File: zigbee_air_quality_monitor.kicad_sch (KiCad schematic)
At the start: 21 parts, among them J1 USB_C_Receptacle_USB2.0, J2 Conn_02x02_Odd_Even, SW1 PWR_BTN, U1 BT840, U2 PRTR5V0U2F, U3 XC6206P332MR, U4 SCD41-D-R2

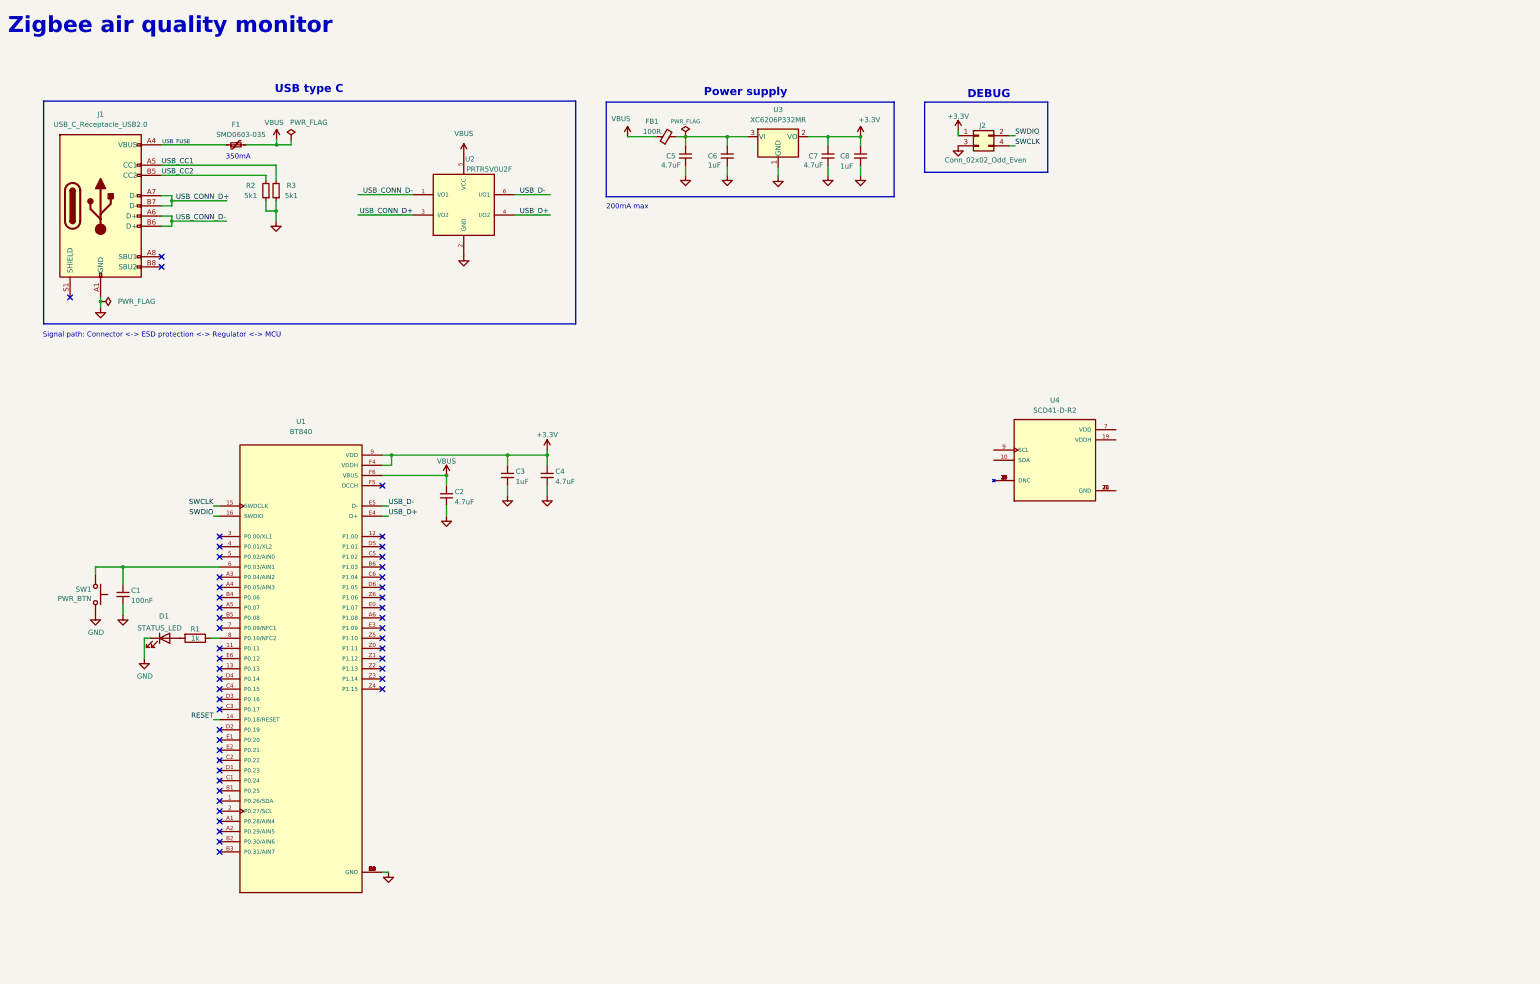
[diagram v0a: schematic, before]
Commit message: Finished schematics, added 3D models
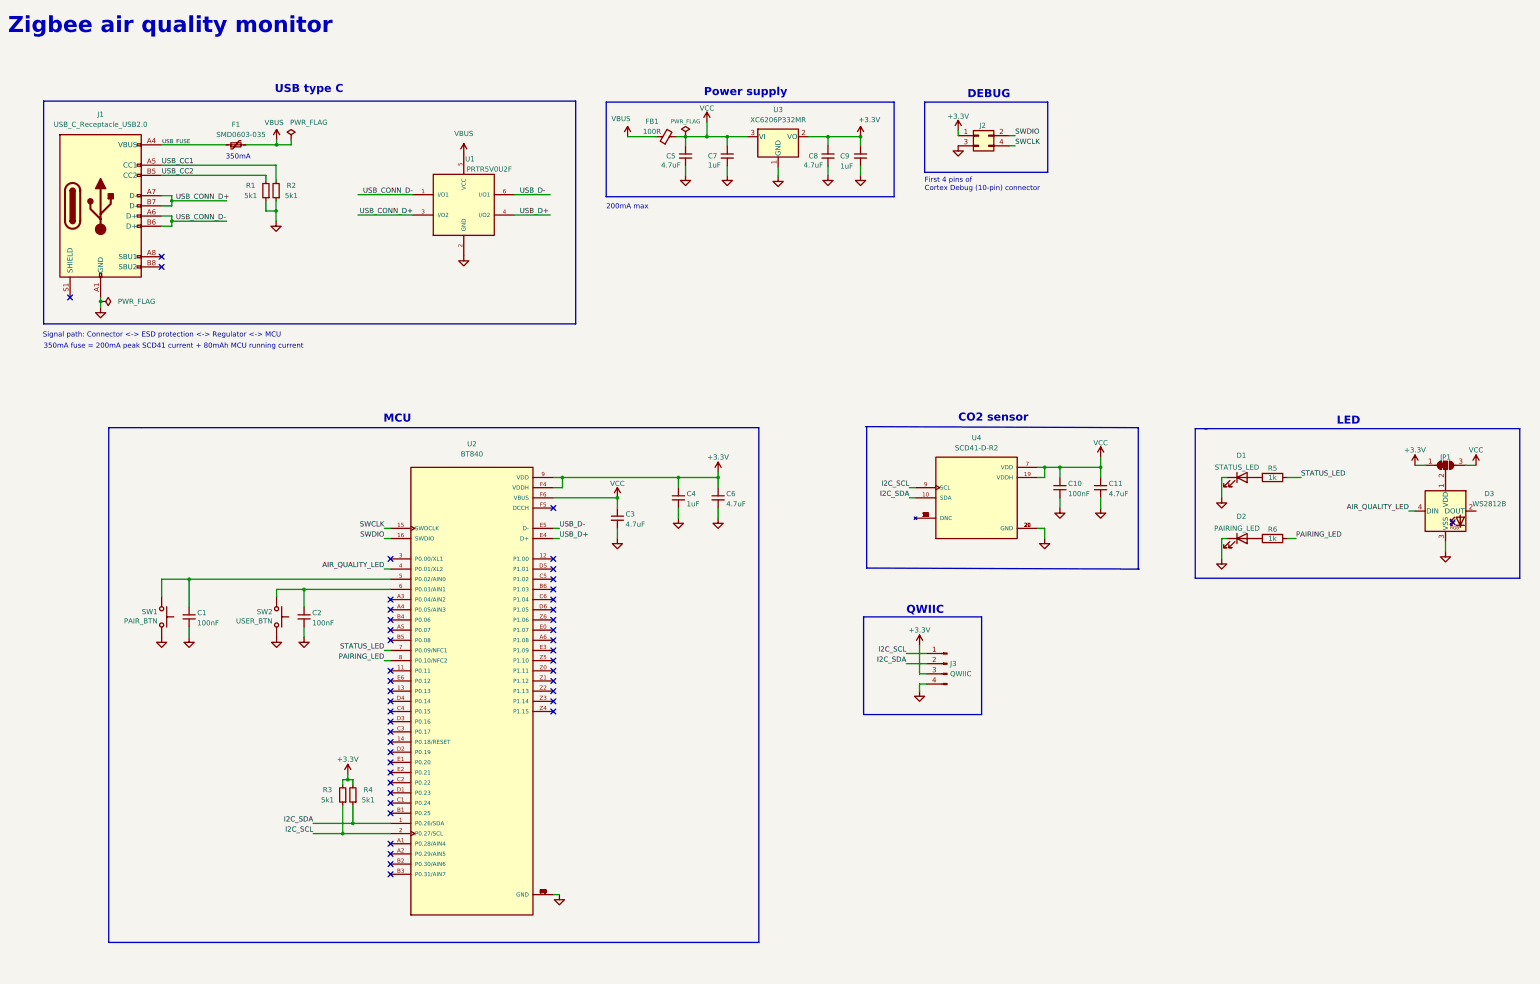
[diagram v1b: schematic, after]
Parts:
- added C1, C10: 100nF, Capacitor_SMD:C_0603_1608Metric, symbol Device:C_Small
- added C11: 4.7uF, Capacitor_SMD:C_0603_1608Metric, symbol Device:C_Small
- added D1: STATUS_LED, LED_SMD:LED_0603_1608Metric, symbol Device:LED
- added D3: WS2812B, LED_SMD:LED_WS2812B-2020_PLCC4_2.0x2.0mm, symbol LED:WS2812B
- added J3: QWIIC, Connector_JST:JST_SH_BM04B-SRSS-TB_1x04-1MP_P1.00mm_Vertical, symbol Connector:Conn_01x04_Male
- added JP1: SolderJumper_3_Bridged12, Jumper:SolderJumper-3_P1.3mm_Open_RoundedPad1.0x1.5mm, symbol Jumper:SolderJumper_3_Bridged12
- added R3, R4: 5k1, Resistor_SMD:R_0603_1608Metric, symbol Device:R_Small
- added R5: 1k, Resistor_SMD:R_0603_1608Metric, symbol Device:R
- added SW1: PAIR_BTN, Button_Switch_SMD:SW_Push_SPST_NO_Alps_SKRK, symbol Switch:SW_Push
- D2: renamed from D1; value STATUS_LED -> PAIRING_LED
- SW2: renamed from SW1; value PWR_BTN -> USER_BTN; footprint Button_Switch_SMD:SW_Push_1P1T_NO_6x6mm_H9.5mm -> Button_Switch_SMD:SW_Push_SPST_NO_Alps_SKRK; LCSC Part (none) -> C115357
- renumbered C1 to C2, C2 to C3, C3 to C4, C4 to C6, C6 to C7, C7 to C8, C8 to C9, R2 to R1, R3 to R2, R1 to R6, U2 to U1, U1 to U2
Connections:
- net +3.3V: now also J3.3 (Pin_3), JP1.1 (A), R3.2, R4.2
- net GND: now also U4.20 (GND), U4.21 (GND), U4.6 (GND), C1.2, C10.2, C11.2, D1.1 (K), D3.3 (VSS), J3.4 (Pin_4), SW1.2
- net VBUS: no longer C3.1, U2.F6 (VBUS)
- net VCC: now reaches C5.1, C7.1, FB1.2, U3.3 (VI)
- net VCC: now also C3.1, U2.F6 (VBUS), U4.19 (VDDH), U4.7 (VDD), C10.1, C11.1, JP1.3 (B)
- net I2C_SDA: now reaches U2.1 (P0.26/SDA)
- net I2C_SDA: now also U4.10 (SDA), J3.2 (Pin_2), R4.1
- net I2C_SCL: now reaches U2.2 (P0.27/SCL)
- net I2C_SCL: now also U4.9 (SCL), J3.1 (Pin_1), R3.1
- net AIR_QUALITY_LED: now reaches U2.4 (P0.01/XL2)
- net AIR_QUALITY_LED: now also D3.4 (DIN)
- net at U2.5 (P0.02/AIN0): now also C1.1, SW1.1
- net STATUS_LED: now reaches U2.7 (P0.09/NFC1)
- net STATUS_LED: now also R5.1
- net PAIRING_LED: now reaches R6.1, U2.8 (P0.10/NFC2)
- net RESET: no longer names the net of U2.14 (P0.18/RESET)
- new net: D3.1 (VDD), JP1.2 (C)
- new net: D1.2 (A), R5.2
- no-connect marks 49 -> 46
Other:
- note added: "350mA fuse = 200mA peak SCD41 current + 80mAh MCU running current"
- note added: "CO2 sensor"
- note added: "First 4 pins of Cortex Debug (10-pin) connector"
- note added: "LED"
- note added: "MCU"
- note added: "QWIIC"
- moved on the sheet: C2, C3, C4, C6, D2, R6, SW2, U2, U4

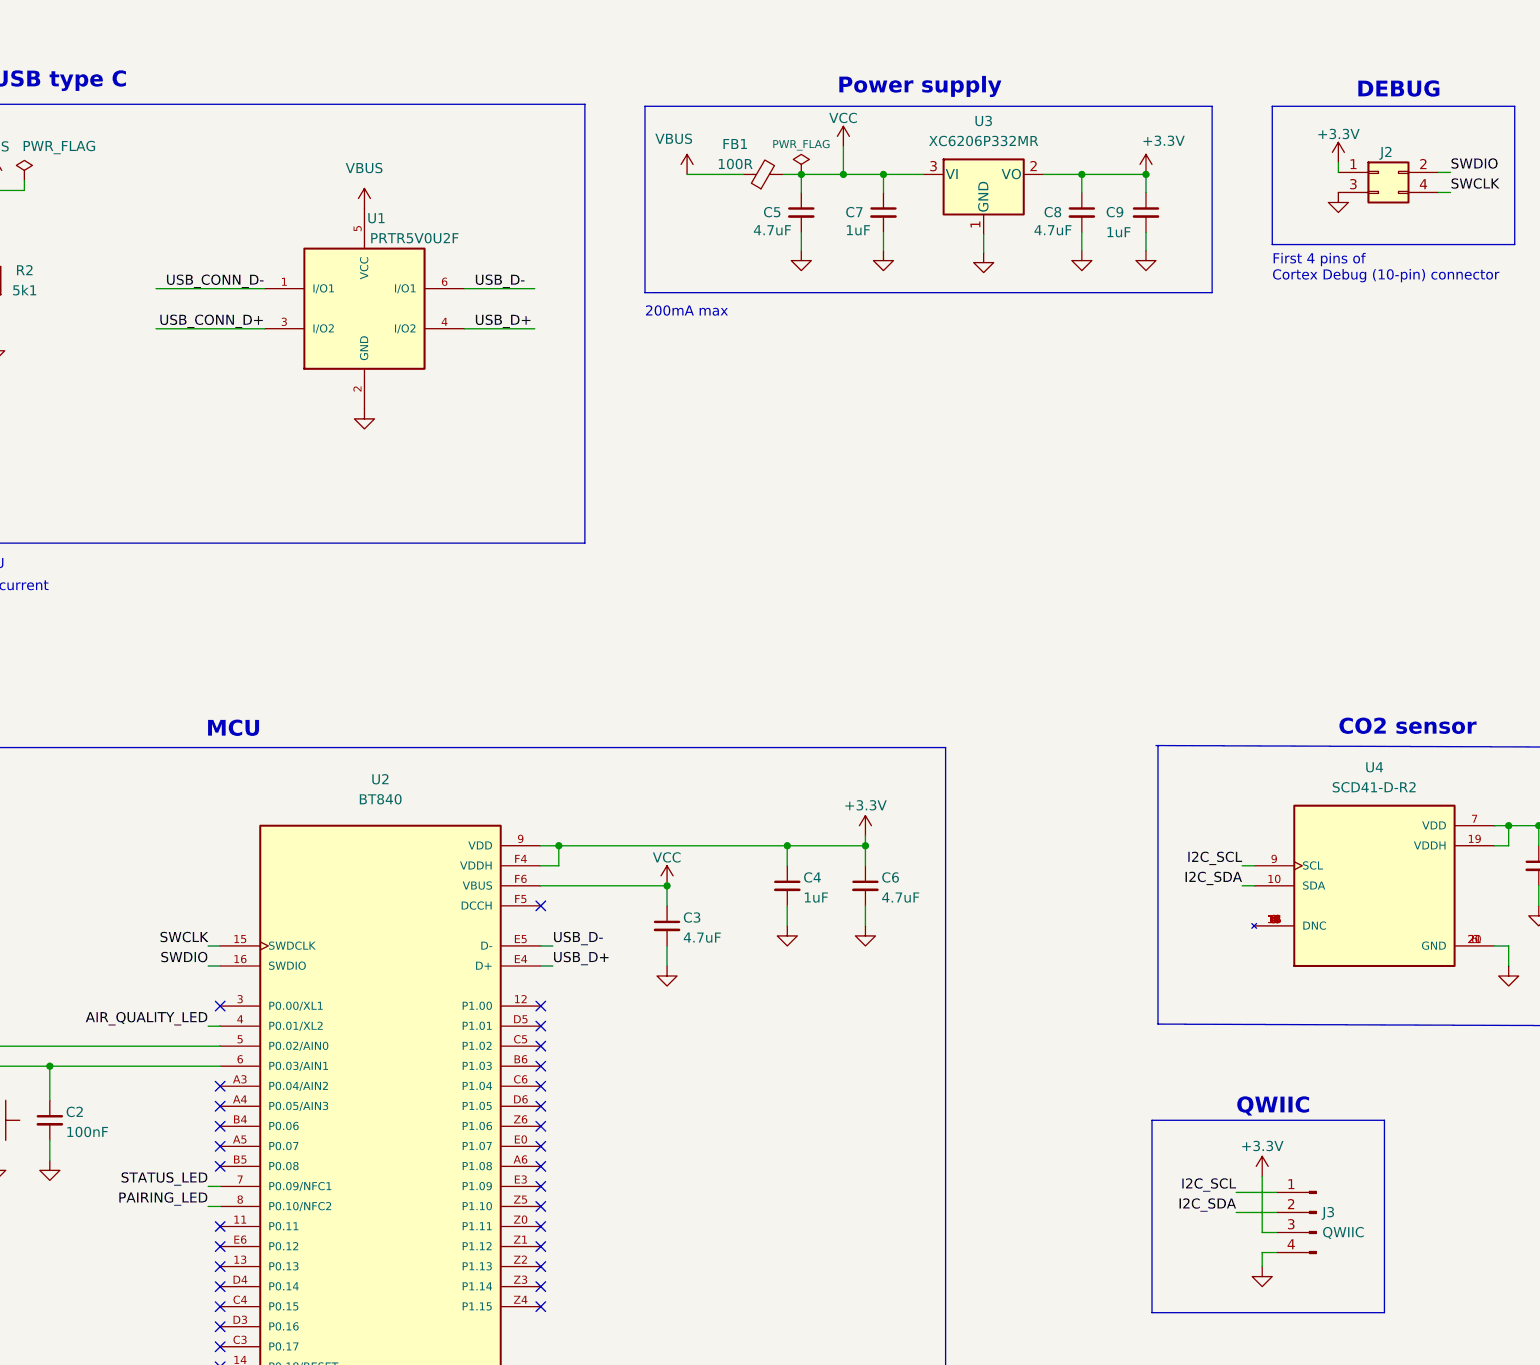
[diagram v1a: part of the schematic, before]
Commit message: Rough part placement
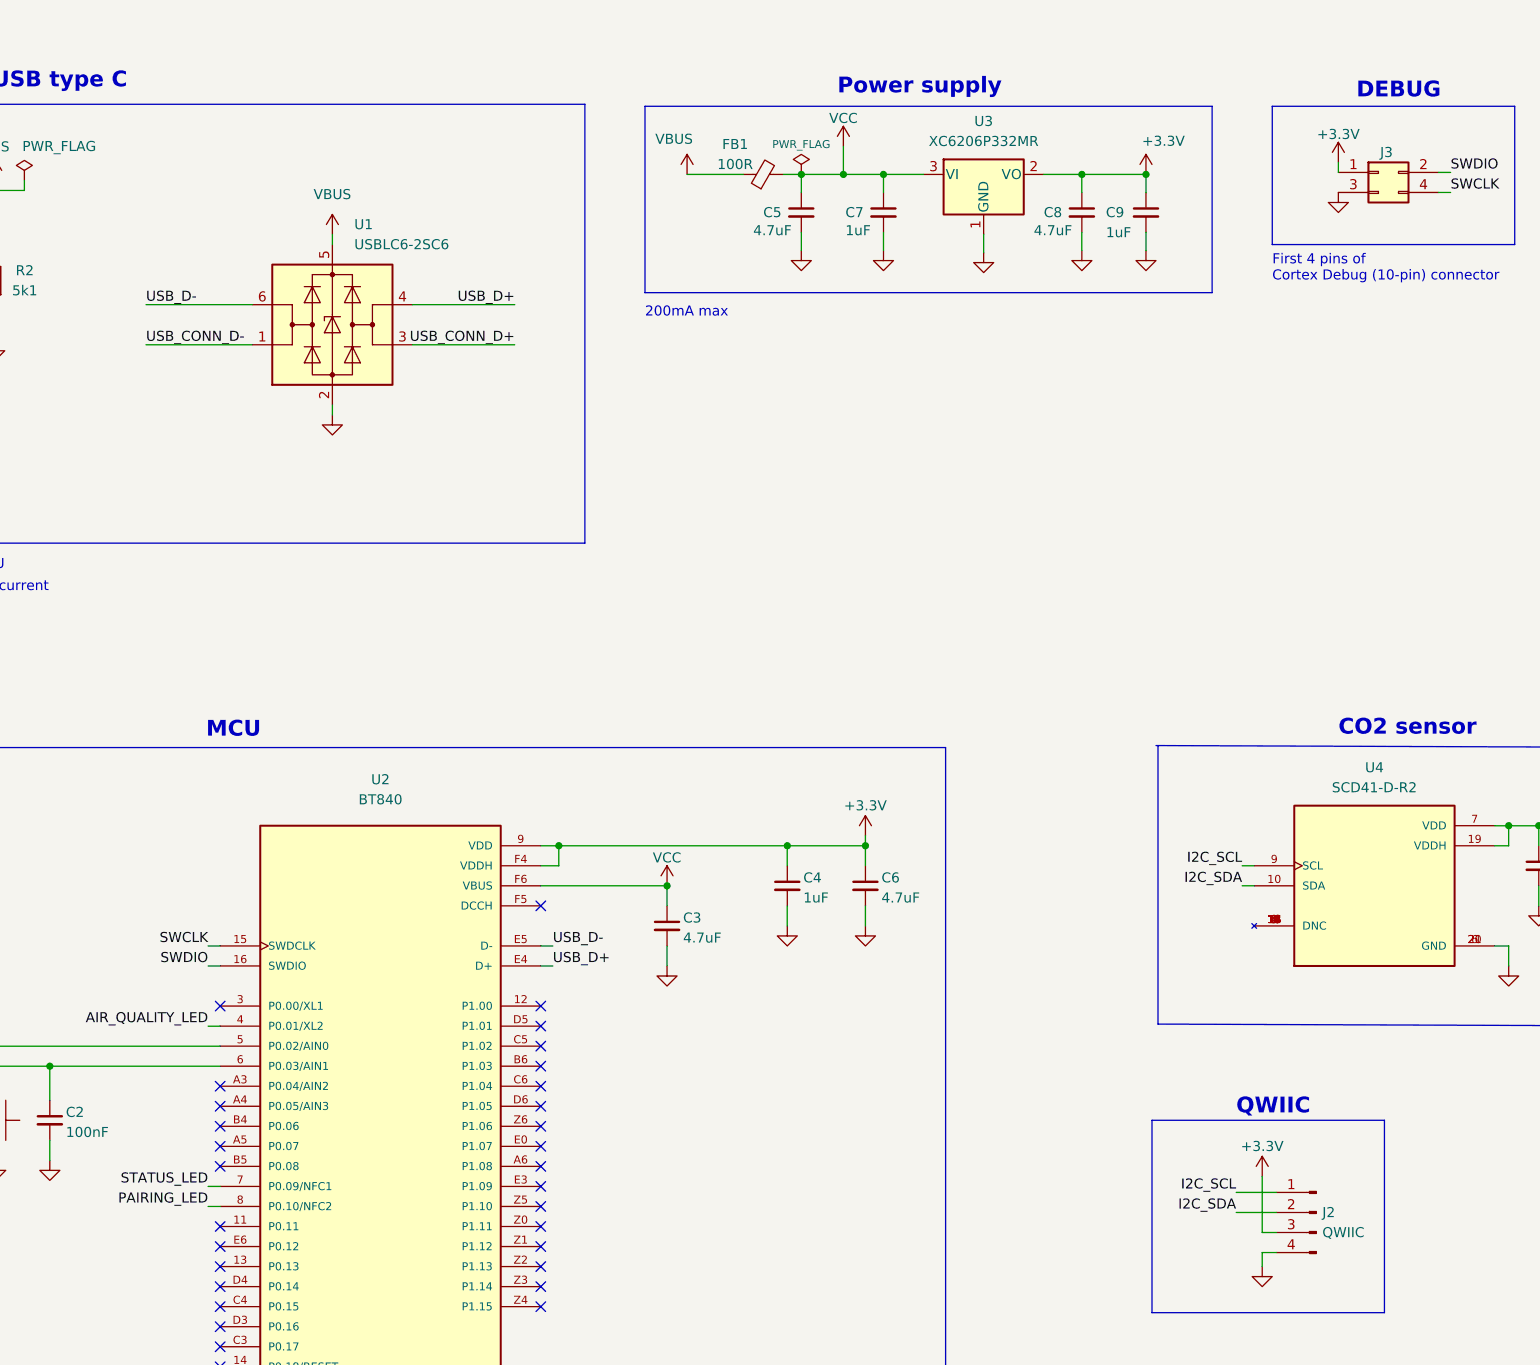
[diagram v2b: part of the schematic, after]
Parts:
- removed U1: PRTR5V0U2F, zigbee_air_quality_monitor:PSON50P145X100X90-6N, symbol zigbee_air_quality_monitor:PRTR5V0U2F
- added U1: USBLC6-2SC6, Package_TO_SOT_SMD:SOT-23-6, symbol Power_Protection:USBLC6-2SC6
- J2: renamed from J3; LCSC Part (none) -> C160404
- renumbered J2 to J3
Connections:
- net GND: now also U1.2 (GND)
- net USB_CONN_D+: now also U1.3 (I/O2)
- net USB_CONN_D-: now also U1.1 (I/O1)
- net USB_D+: now also U1.4 (I/O2)
- net USB_D-: now also U1.6 (I/O1)
- net VBUS: now also U1.5 (VBUS)

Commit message: Routing WIP
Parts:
- removed JP1: SolderJumper_3_Bridged12, Jumper:SolderJumper-3_P1.3mm_Open_RoundedPad1.0x1.5mm, symbol Jumper:SolderJumper_3_Bridged12
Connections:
- net +3.3V: now also D3.1 (VDD)
- net PAIRING_LED: now also U2.14 (P0.18/RESET); no longer U2.8 (P0.10/NFC2)
- net STATUS_LED: now also U2.13 (P0.13); no longer U2.7 (P0.09/NFC1)
- net USB_CONN_D+: now also J1.A6 (D+), J1.B6 (D+), U1.1 (I/O1); no longer J1.A7 (D-), J1.B7 (D-), U1.3 (I/O2)
- net USB_CONN_D-: now also J1.A7 (D-), J1.B7 (D-), U1.3 (I/O2); no longer J1.A6 (D+), J1.B6 (D+), U1.1 (I/O1)
- net USB_D+: now also U1.6 (I/O1); no longer U1.4 (I/O2)
- net USB_D-: now also U1.4 (I/O2); no longer U1.6 (I/O1)
- no-connect marks 46 -> 47
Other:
- note added: "NFC pins are not suitable for >=10MHz operation, it can interfere with radio communication. When using PWM on these pins, lower the frequency. There is also some leaking current when they have different levels and CPU is in sleep mode."

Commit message: All parts routed
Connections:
- net PAIRING_LED: now also U2.5 (P0.02/AIN0); no longer U2.14 (P0.18/RESET)
- net at C1.1, SW1.1: now also U2.7 (P0.09/NFC1); no longer U2.5 (P0.02/AIN0)
- net at C2.1, SW2.1: now also U2.8 (P0.10/NFC2); no longer U2.6 (P0.03/AIN1)
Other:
- moved on the sheet: C1, C2, SW1, SW2
